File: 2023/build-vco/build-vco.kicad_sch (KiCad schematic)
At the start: 3 parts, among them M1 PMOS_OR1, M2 PMOS_OR1, M27 NMOS_OR1

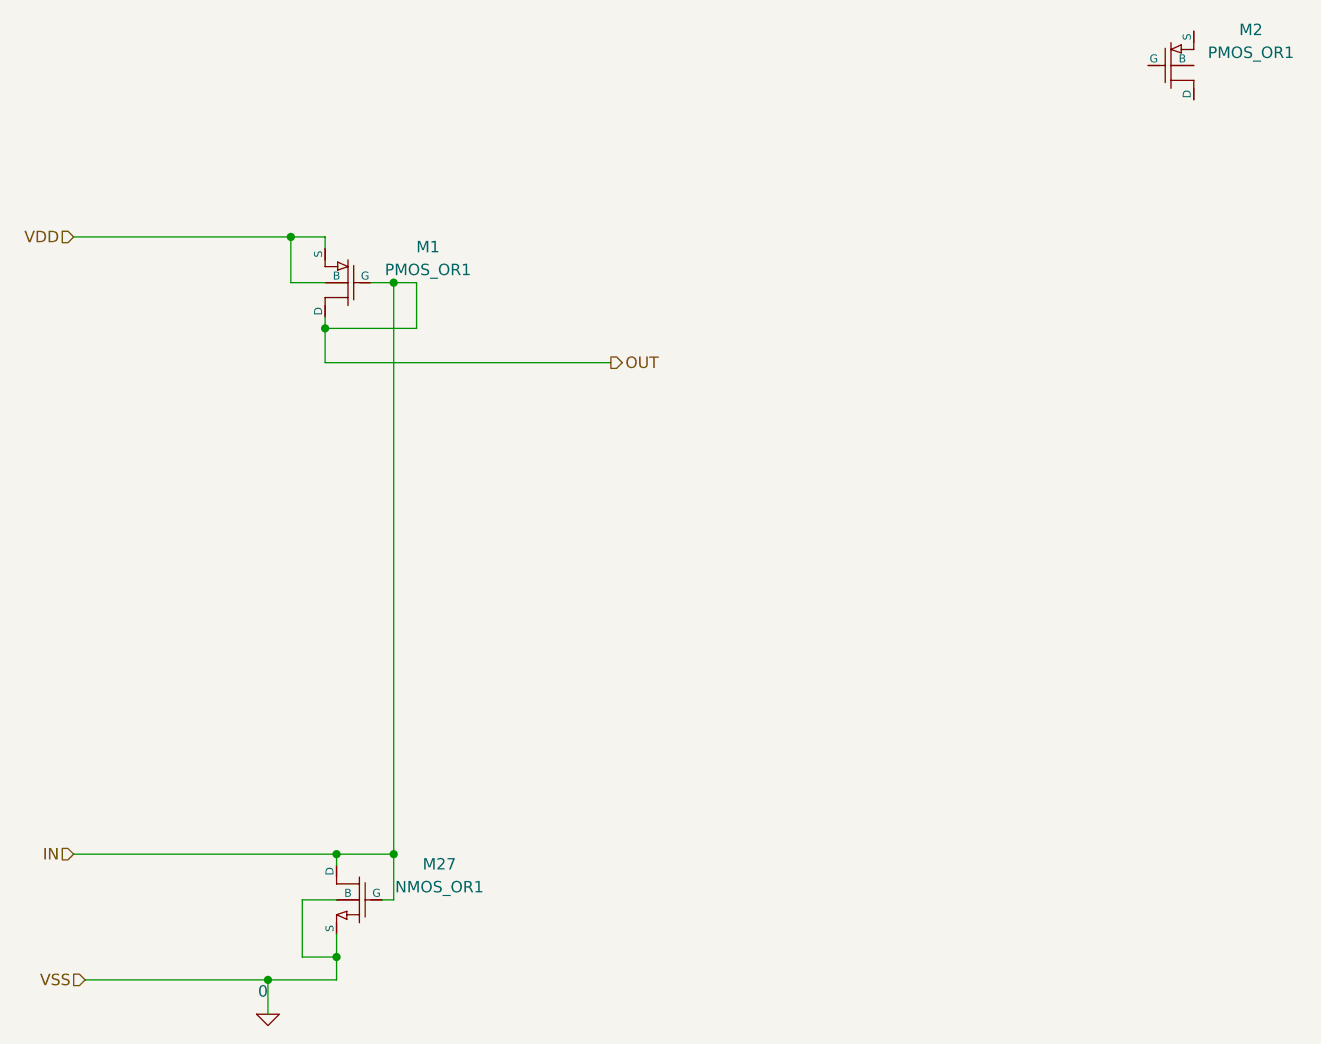
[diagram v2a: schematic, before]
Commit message: PMOS x 1, NMOS x 2 で LVS OK.
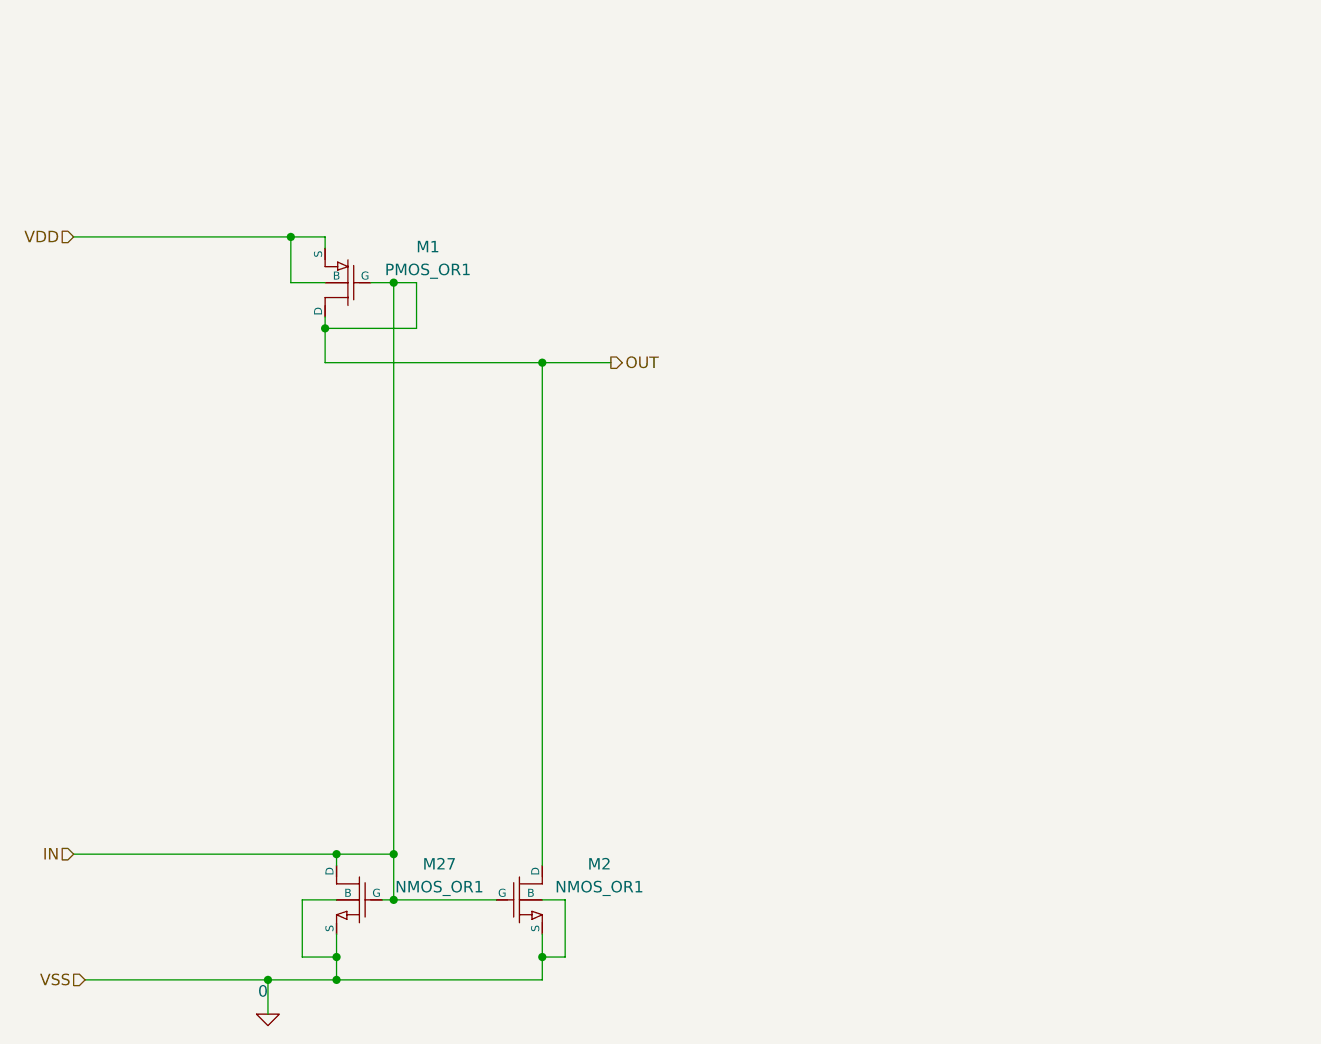
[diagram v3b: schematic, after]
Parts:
- removed M2: PMOS_OR1, symbol OR1Symbols:PMOS_OR1
- added M2: NMOS_OR1, symbol OR1Symbols:NMOS_OR1
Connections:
- net 0: now also M2.3 (S), M2.4 (B)
- net IN: now also M2.1 (D), M2.2 (G)
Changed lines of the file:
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@@
   (junction (at 133.35 123.19) (diameter 0) (color 0 0 0 0)
   )
+  (junction (at 156.21 134.62) (diameter 0) (color 0 0 0 0)
+  )
   (junction (at 139.7 59.69) (diameter 0) (color 0 0 0 0)
   )
+  (junction (at 156.21 68.58) (diameter 0) (color 0 0 0 0)
+  )
+  (junction (at 139.7 128.27) (diameter 0) (color 0 0 0 0)
+  )
   (junction (at 139.7 123.19) (diameter 0) (color 0 0 0 0)
   )
@@
   (junction (at 128.27 54.61) (diameter 0) (color 0 0 0 0)
   )
+  (junction (at 133.35 137.16) (diameter 0) (color 0 0 0 0)
+  )
   (junction (at 125.73 137.16) (diameter 0) (color 0 0 0 0)
   )
@@
     (stroke (width 0) (type default))
   )
+  (wire (pts (xy 156.21 134.62) (xy 158.75 134.62))
+    (stroke (width 0) (type default))
+  )
   (wire (pts (xy 125.73 137.16) (xy 125.73 140.97))
     (stroke (width 0) (type default))
@@
     (stroke (width 0) (type default))
   )
+  (wire (pts (xy 156.21 68.58) (xy 163.83 68.58))
+    (stroke (width 0) (type default))
+  )
   (wire (pts (xy 142.24 64.77) (xy 132.08 64.77))
     (stroke (width 0) (type default))
   )
+  (wire (pts (xy 139.7 128.27) (xy 151.13 128.27))
+    (stroke (width 0) (type default))
+  )
   (wire (pts (xy 129.54 128.27) (xy 129.54 134.62))
     (stroke (width 0) (type default))
@@
     (stroke (width 0) (type default))
   )
+  (wire (pts (xy 156.21 132.08) (xy 156.21 134.62))
+    (stroke (width 0) (type default))
+  )
   (wire (pts (xy 129.54 134.62) (xy 133.35 134.62))
     (stroke (width 0) (type default))
@@
     (stroke (width 0) (type default))
   )
+  (wire (pts (xy 156.21 134.62) (xy 156.21 137.16))
+    (stroke (width 0) (type default))
+  )
+  (wire (pts (xy 156.21 128.27) (xy 158.75 128.27))
+    (stroke (width 0) (type default))
+  )
+  (wire (pts (xy 158.75 128.27) (xy 158.75 134.62))
+    (stroke (width 0) (type default))
+  )
   (wire (pts (xy 139.7 59.69) (xy 142.24 59.69))
     (stroke (width 0) (type default))
@@
     (stroke (width 0) (type default))
   )
-  (wire (pts (xy 132.08 68.58) (xy 163.83 68.58))
+  (wire (pts (xy 156.21 68.58) (xy 156.21 124.46))
+    (stroke (width 0) (type default))
+  )
+  (wire (pts (xy 156.21 137.16) (xy 133.35 137.16))
+    (stroke (width 0) (type default))
+  )
+  (wire (pts (xy 132.08 68.58) (xy 156.21 68.58))
     (stroke (width 0) (type default))
   )
@@
     )
   )
-  (symbol (lib_id "OR1Symbols:PMOS_OR1") (at 223.52 35.56 0) (unit 1)
+  (symbol (lib_name "NMOS_OR1_1") (lib_id "OR1Symbols:NMOS_OR1") (at 151.13 128.27 0) (unit 1)
     (in_bom yes) (on_board yes) (dnp no) (fields_autoplaced)
-    (property "Reference" "M2" (at 234.95 31.5977 0)
-      (effects (font (size 1.27 1.27)))
-    )
-    (property "Value" "PMOS_OR1" (at 234.95 34.1377 0)
-      (effects (font (size 1.27 1.27)))
-    )
-    (property "Footprint" "" (at 223.52 35.56 0)
-      (effects (font (size 1.27 1.27)) hide)
-    )
-    (property "Datasheet" "" (at 223.52 35.56 0)
-      (effects (font (size 1.27 1.27)) hide)
-    )
-    (property "Sim.Pins" "1=1 2=2 3=3 4=4" (at 223.52 35.56 0)
-      (effects (font (size 1.27 1.27)) hide)
-    )
-    (property "Sim.Device" "SPICE" (at 232.41 40.64 0)
+    (property "Reference" "M2" (at 162.56 124.3077 0)
+      (effects (font (size 1.27 1.27)))
+    )
+    (property "Value" "NMOS_OR1" (at 162.56 126.8477 0)
+      (effects (font (size 1.27 1.27)))
+    )
+    (property "Footprint" "" (at 151.13 128.27 0)
+      (effects (font (size 1.27 1.27)) hide)
+    )
+    (property "Datasheet" "" (at 151.13 128.27 0)
+      (effects (font (size 1.27 1.27)) hide)
+    )
+    (property "Sim.Pins" "1=1 2=2 3=3 4=4" (at 151.13 128.27 0)
+      (effects (font (size 1.27 1.27)) hide)
+    )
+    (property "Sim.Device" "SPICE" (at 160.02 133.35 0)
       (effects (font (size 1.27 1.27)) (justify left) hide)
     )
-    (property "Sim.Params" "type=\"M\" model=\"PMOS_OR1 l=1u w=6u\" lib=\"\"" (at 223.52 35.56 0)
-      (effects (font (size 1.27 1.27)) hide)
-    )
+    (property "Sim.Params" "type=\"M\" model=\"NMOS_OR1 l=1u w=2u\" lib=\"\"" (at 151.13 128.27 0)
+      (effects (font (size 1.27 1.27)) hide)
+    )

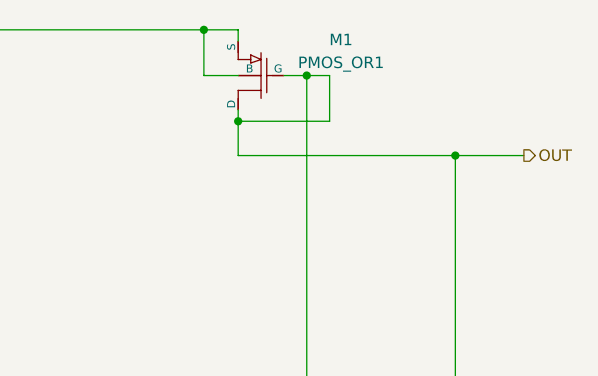
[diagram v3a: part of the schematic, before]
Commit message: PMOS x 2, NMOS x 2 で LVS は OK.
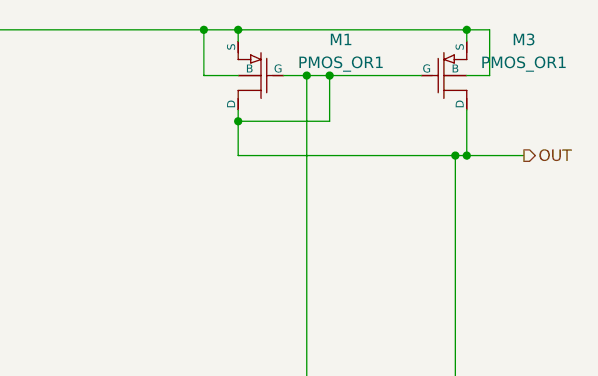
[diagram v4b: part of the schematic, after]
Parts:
- added M3: PMOS_OR1, symbol OR1Symbols:PMOS_OR1
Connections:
- net IN: now also M3.1 (D), M3.2 (G)
- net VDD: now also M3.3 (S), M3.4 (B)
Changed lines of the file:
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@@
   (junction (at 133.35 123.19) (diameter 0) (color 0 0 0 0)
   )
+  (junction (at 157.48 68.58) (diameter 0) (color 0 0 0 0)
+  )
   (junction (at 156.21 134.62) (diameter 0) (color 0 0 0 0)
   )
@@
   (junction (at 156.21 68.58) (diameter 0) (color 0 0 0 0)
   )
+  (junction (at 142.24 59.69) (diameter 0) (color 0 0 0 0)
+  )
   (junction (at 139.7 128.27) (diameter 0) (color 0 0 0 0)
   )
@@
   (junction (at 132.08 64.77) (diameter 0) (color 0 0 0 0)
   )
+  (junction (at 132.08 54.61) (diameter 0) (color 0 0 0 0)
+  )
   (junction (at 133.35 134.62) (diameter 0) (color 0 0 0 0)
   )
@@
   (junction (at 133.35 137.16) (diameter 0) (color 0 0 0 0)
   )
+  (junction (at 157.48 54.61) (diameter 0) (color 0 0 0 0)
+  )
   (junction (at 125.73 137.16) (diameter 0) (color 0 0 0 0)
   )
@@
     (stroke (width 0) (type default))
   )
+  (wire (pts (xy 157.48 54.61) (xy 160.02 54.61))
+    (stroke (width 0) (type default))
+  )
   (wire (pts (xy 139.7 59.69) (xy 139.7 123.19))
     (stroke (width 0) (type default))
   )
-  (wire (pts (xy 156.21 68.58) (xy 163.83 68.58))
+  (wire (pts (xy 156.21 68.58) (xy 157.48 68.58))
     (stroke (width 0) (type default))
   )
@@
     (stroke (width 0) (type default))
   )
+  (wire (pts (xy 160.02 59.69) (xy 160.02 54.61))
+    (stroke (width 0) (type default))
+  )
   (wire (pts (xy 139.7 128.27) (xy 151.13 128.27))
     (stroke (width 0) (type default))
@@
     (stroke (width 0) (type default))
   )
+  (wire (pts (xy 132.08 54.61) (xy 157.48 54.61))
+    (stroke (width 0) (type default))
+  )
+  (wire (pts (xy 157.48 54.61) (xy 157.48 55.88))
+    (stroke (width 0) (type default))
+  )
   (wire (pts (xy 156.21 134.62) (xy 156.21 137.16))
     (stroke (width 0) (type default))
@@
     (stroke (width 0) (type default))
   )
+  (wire (pts (xy 157.48 68.58) (xy 163.83 68.58))
+    (stroke (width 0) (type default))
+  )
+  (wire (pts (xy 157.48 63.5) (xy 157.48 68.58))
+    (stroke (width 0) (type default))
+  )
   (wire (pts (xy 139.7 59.69) (xy 142.24 59.69))
     (stroke (width 0) (type default))
   )
+  (wire (pts (xy 157.48 59.69) (xy 160.02 59.69))
+    (stroke (width 0) (type default))
+  )
   (wire (pts (xy 142.24 59.69) (xy 142.24 64.77))
     (stroke (width 0) (type default))
@@
   )
   (wire (pts (xy 133.35 134.62) (xy 133.35 137.16))
+    (stroke (width 0) (type default))
+  )
+  (wire (pts (xy 142.24 59.69) (xy 152.4 59.69))
     (stroke (width 0) (type default))
   )
@@
         )
       )
+    )
+  )
+  (symbol (lib_name "PMOS_OR1_1") (lib_id "OR1Symbols:PMOS_OR1") (at 152.4 59.69 0) (unit 1)
+    (in_bom yes) (on_board yes) (dnp no) (fields_autoplaced)
+    (property "Reference" "M3" (at 163.83 55.7277 0)
+      (effects (font (size 1.27 1.27)))
+    )
+    (property "Value" "PMOS_OR1" (at 163.83 58.2677 0)
+      (effects (font (size 1.27 1.27)))
+    )
+    (property "Footprint" "" (at 152.4 59.69 0)
+      (effects (font (size 1.27 1.27)) hide)
+    )
+    (property "Datasheet" "" (at 152.4 59.69 0)
+      (effects (font (size 1.27 1.27)) hide)
+    )
+    (property "Sim.Pins" "1=1 2=2 3=3 4=4" (at 152.4 59.69 0)
+      (effects (font (size 1.27 1.27)) hide)
+    )
+    (property "Sim.Device" "SPICE" (at 161.29 64.77 0)
+      (effects (font (size 1.27 1.27)) (justify left) hide)
+    )
+    (property "Sim.Params" "type=\"M\" model=\"PMOS_OR1 l=1u w=6u\" lib=\"\"" (at 152.4 59.69 0)
+      (effects (font (size 1.27 1.27)) hide)
+    )
+    (pin "1")
+    (pin "2")
+    (pin "3")
+    (pin "4")
+    (instances
+      (project "build-vco"
+        (path "/178e7a69-f569-4b69-ab89-e6b9cdb6309f"
+          (reference "M3") (unit 1)
+        )
+      )

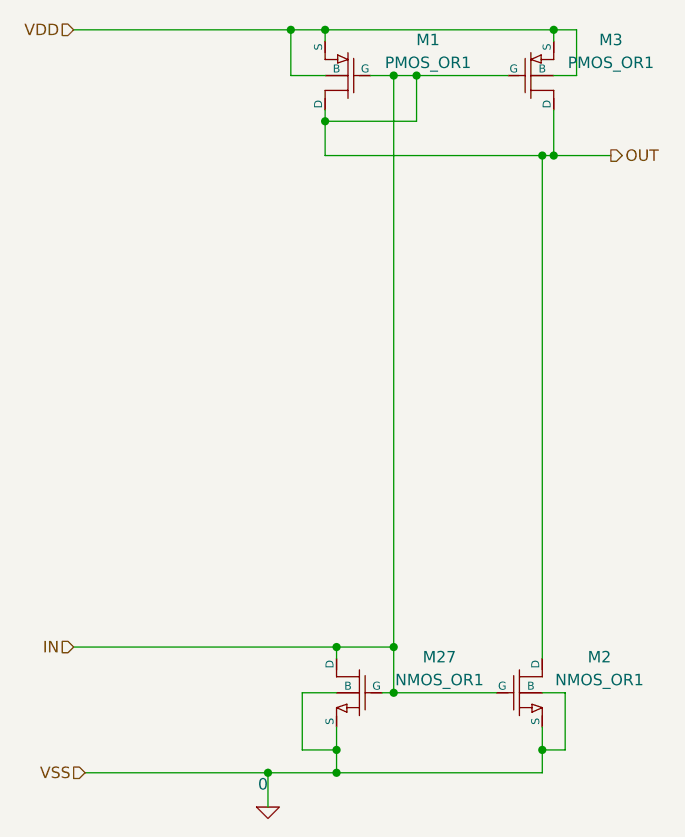
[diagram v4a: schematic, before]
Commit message: PMOS x 2, NMOS x 3 で LVS は OK.
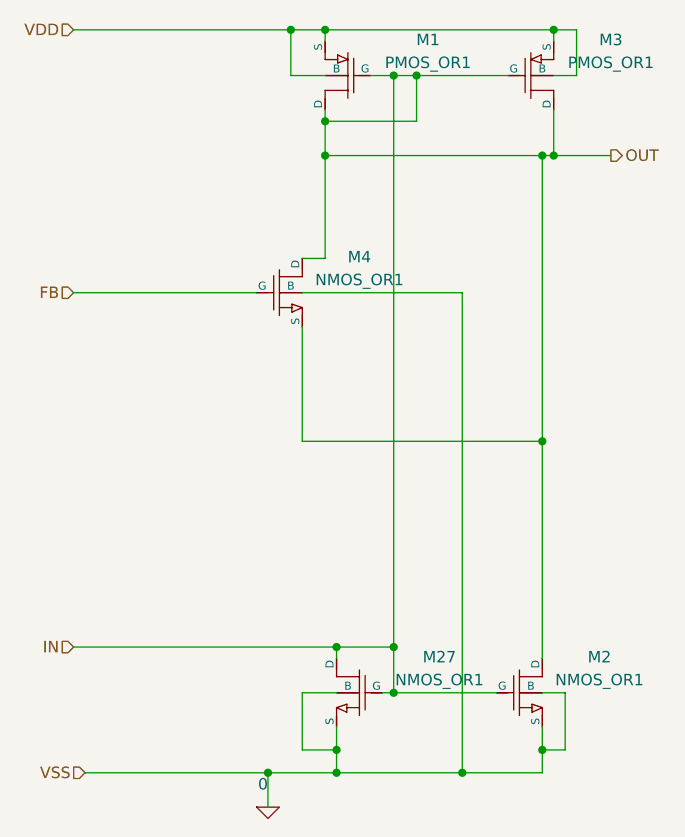
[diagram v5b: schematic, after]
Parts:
- added M4: NMOS_OR1, symbol OR1Symbols:NMOS_OR1
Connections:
- net 0: now also M4.4 (B)
- net IN: now also M4.1 (D), M4.3 (S)
- new net FB: M4.2 (G)
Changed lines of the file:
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@@
   (junction (at 156.21 68.58) (diameter 0) (color 0 0 0 0)
   )
+  (junction (at 156.21 100.33) (diameter 0) (color 0 0 0 0)
+  )
   (junction (at 142.24 59.69) (diameter 0) (color 0 0 0 0)
   )
+  (junction (at 147.32 137.16) (diameter 0) (color 0 0 0 0)
+  )
   (junction (at 139.7 128.27) (diameter 0) (color 0 0 0 0)
   )
@@
   (junction (at 157.48 54.61) (diameter 0) (color 0 0 0 0)
   )
+  (junction (at 132.08 68.58) (diameter 0) (color 0 0 0 0)
+  )
   (junction (at 125.73 137.16) (diameter 0) (color 0 0 0 0)
   )
@@
     (stroke (width 0) (type default))
   )
+  (wire (pts (xy 132.08 68.58) (xy 132.08 80.01))
+    (stroke (width 0) (type default))
+  )
   (wire (pts (xy 139.7 123.19) (xy 139.7 128.27))
     (stroke (width 0) (type default))
@@
     (stroke (width 0) (type default))
   )
+  (wire (pts (xy 129.54 83.82) (xy 147.32 83.82))
+    (stroke (width 0) (type default))
+  )
+  (wire (pts (xy 147.32 83.82) (xy 147.32 137.16))
+    (stroke (width 0) (type default))
+  )
   (wire (pts (xy 157.48 54.61) (xy 160.02 54.61))
     (stroke (width 0) (type default))
@@
     (stroke (width 0) (type default))
   )
+  (wire (pts (xy 129.54 87.63) (xy 129.54 100.33))
+    (stroke (width 0) (type default))
+  )
   (wire (pts (xy 125.73 137.16) (xy 133.35 137.16))
     (stroke (width 0) (type default))
@@
     (stroke (width 0) (type default))
   )
+  (wire (pts (xy 129.54 80.01) (xy 132.08 80.01))
+    (stroke (width 0) (type default))
+  )
   (wire (pts (xy 137.16 59.69) (xy 139.7 59.69))
     (stroke (width 0) (type default))
@@
     (stroke (width 0) (type default))
   )
+  (wire (pts (xy 104.14 83.82) (xy 124.46 83.82))
+    (stroke (width 0) (type default))
+  )
   (wire (pts (xy 128.27 59.69) (xy 128.27 54.61))
     (stroke (width 0) (type default))
   )
+  (wire (pts (xy 147.32 137.16) (xy 133.35 137.16))
+    (stroke (width 0) (type default))
+  )
   (wire (pts (xy 132.08 59.69) (xy 128.27 59.69))
     (stroke (width 0) (type default))
@@
     (stroke (width 0) (type default))
   )
+  (wire (pts (xy 156.21 100.33) (xy 156.21 124.46))
+    (stroke (width 0) (type default))
+  )
   (wire (pts (xy 157.48 54.61) (xy 157.48 55.88))
     (stroke (width 0) (type default))
@@
     (stroke (width 0) (type default))
   )
+  (wire (pts (xy 129.54 100.33) (xy 156.21 100.33))
+    (stroke (width 0) (type default))
+  )
   (wire (pts (xy 157.48 59.69) (xy 160.02 59.69))
     (stroke (width 0) (type default))
@@
     (stroke (width 0) (type default))
   )
-  (wire (pts (xy 156.21 68.58) (xy 156.21 124.46))
-    (stroke (width 0) (type default))
-  )
-  (wire (pts (xy 156.21 137.16) (xy 133.35 137.16))
+  (wire (pts (xy 156.21 68.58) (xy 156.21 100.33))
+    (stroke (width 0) (type default))
+  )
+  (wire (pts (xy 156.21 137.16) (xy 147.32 137.16))
     (stroke (width 0) (type default))
   )
@@
   )
   (hierarchical_label "IN" (shape input) (at 104.14 123.19 180) (fields_autoplaced)
+    (effects (font (size 1.27 1.27)) (justify right))
+  )
+  (hierarchical_label "FB" (shape input) (at 104.14 83.82 180) (fields_autoplaced)
     (effects (font (size 1.27 1.27)) (justify right))
   )
@@
         )
       )
+    )
+  )
+  (symbol (lib_name "NMOS_OR1_2") (lib_id "OR1Symbols:NMOS_OR1") (at 124.46 83.82 0) (unit 1)
+    (in_bom yes) (on_board yes) (dnp no) (fields_autoplaced)
+    (property "Reference" "M4" (at 135.89 79.8577 0)
+      (effects (font (size 1.27 1.27)))
+    )
+    (property "Value" "NMOS_OR1" (at 135.89 82.3977 0)
+      (effects (font (size 1.27 1.27)))
+    )
+    (property "Footprint" "" (at 124.46 83.82 0)
+      (effects (font (size 1.27 1.27)) hide)
+    )
+    (property "Datasheet" "" (at 124.46 83.82 0)
+      (effects (font (size 1.27 1.27)) hide)
+    )
+    (property "Sim.Pins" "1=1 2=2 3=3 4=4" (at 124.46 83.82 0)
+      (effects (font (size 1.27 1.27)) hide)
+    )
+    (property "Sim.Device" "SPICE" (at 133.35 88.9 0)
+      (effects (font (size 1.27 1.27)) (justify left) hide)
+    )
+    (property "Sim.Params" "type=\"M\" model=\"NMOS_OR1 l=1u w=2u\" lib=\"\"" (at 124.46 83.82 0)
+      (effects (font (size 1.27 1.27)) hide)
+    )
+    (pin "1")
+    (pin "2")
+    (pin "3")
+    (pin "4")
+    (instances
+      (project "build-vco"
+        (path "/178e7a69-f569-4b69-ab89-e6b9cdb6309f"
+          (reference "M4") (unit 1)
+        )
+      )
